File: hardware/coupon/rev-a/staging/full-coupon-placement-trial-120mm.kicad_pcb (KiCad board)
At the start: 2 copper layers, 120 x 32.5 mm, 497 parts, among them J1 USB4505-03-0-A, J2 S2B-PH-SM4-TB, Q1 DMP2066LSN-7, Q10 DMP2066LSN-7, Q11 DMP2066LSN-7, Q12 DMP2066LSN-7, Q13 DMP2066LSN-7, Q14 DMP2066LSN-7, Q15 DMP2066LSN-7, Q16 DMP2066LSN-7, Q17 2N7002K-7, Q18 2N7002K-7, Q19 2N7002K-7, Q2 DMP2066LSN-7, Q20 2N7002K-7, Q21 2N7002K-7, Q22 2N7002K-7, Q23 2N7002K-7, Q24 2N7002K-7, Q25 2N7002K-7, Q26 2N7002K-7, Q27 2N7002K-7, Q28 2N7002K-7, Q29 2N7002K-7, Q3 DMP2066LSN-7, Q30 2N7002K-7, Q31 2N7002K-7, Q32 2N7002K-7, Q4 DMP2066LSN-7, Q5 DMP2066LSN-7, Q6 DMP2066LSN-7, Q7 DMP2066LSN-7, Q8 DMP2066LSN-7, Q9 DMP2066LSN-7, SW1 EVQP7J01P, SW2 JS202011JCQN, U1 TLC59581RTQT, U11 SN74LVC1G04DBVR, U17 SN74LVC1G11DBVR, U2 74HC4514PW,118, U23 SN74LVC1G06DBVR, U24 SN74LVC2G17DBVR, U25 SN74LVC2G17DBVR, U29 TPS70933DBVR, U3 ESP32-S3-WROOM-1U-N16R8, U31 TUSB320LAIRWBR, U32 TS3USB31ERSER, U33 TPD4E05U06DQAR, U34 TPS3808G01DBVR, U35 MAX17048G+T10, U36 TPS631000DRLR, U37 TPS63020DSJT, U38 2.5V shunt, U39 TMP390A2DRLR, U40 SN74AUP1G125DBVR, U41 BQ24074RGTR, U42 SN74AUP1G125DBVR, U43 SN74AUP1G125DBVR, U44 TPS259474ARPWR, U45 TPS259474ARPWR, U46 TCA9517ADGKR, U47 TPS3823A-33DBVR, U48 SN74LVC1G04DSFR, U49 SN74LVC1G74RSER, U50 SN74LVC1G74RSER, U51 SN74LVC1G11DRYR, U52 SN74LVC1G08DSFR, U53 TLV6700DSER, U54 SN74LVC2G00DCUR, U55 SN74LVC2G08DCUR

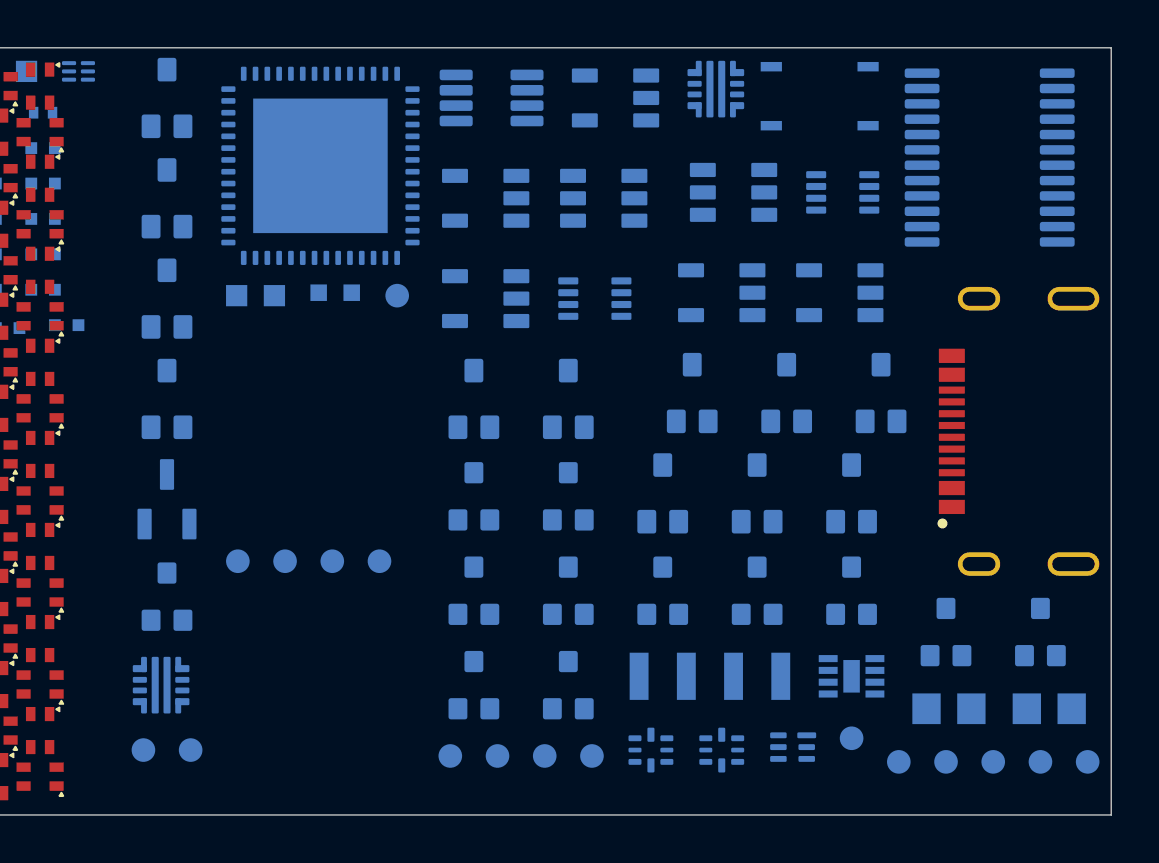
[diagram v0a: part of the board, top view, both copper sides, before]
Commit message: Clear initial placement edge and silkscreen DRC findings
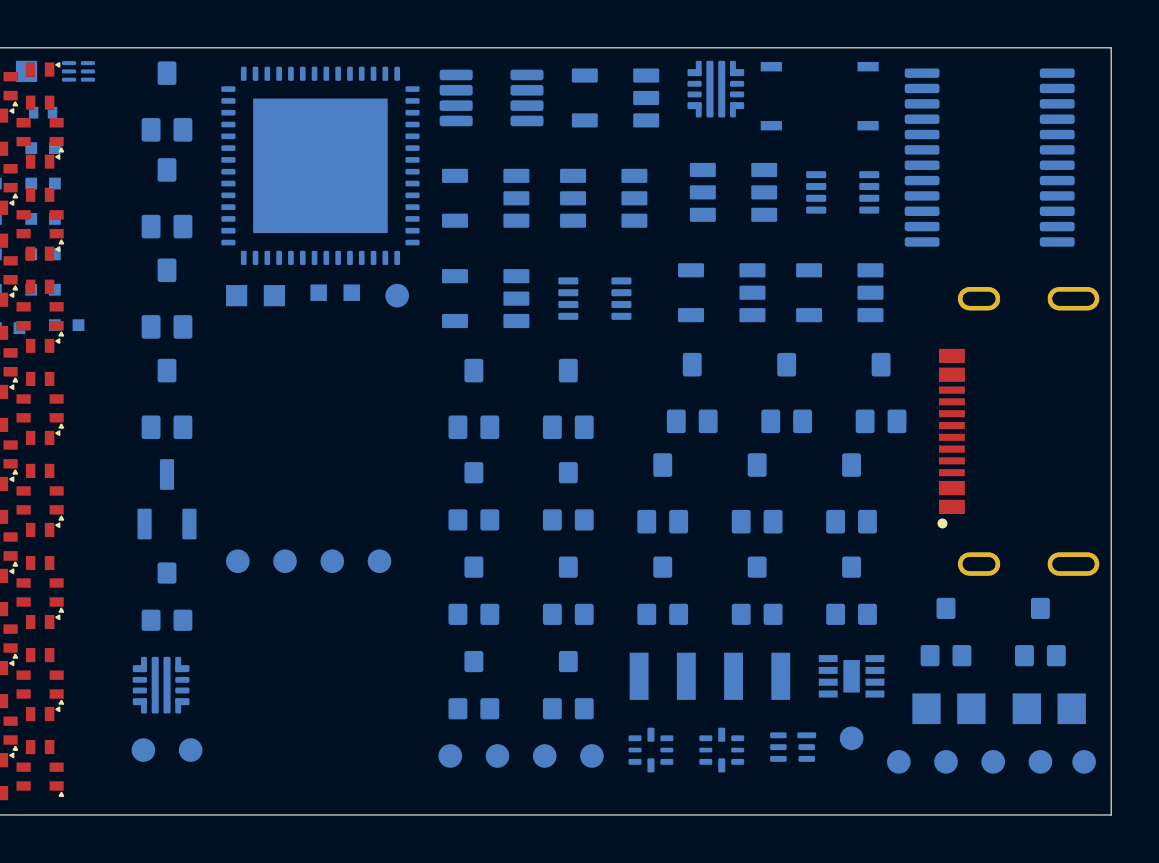
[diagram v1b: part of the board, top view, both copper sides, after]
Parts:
- moved TP4 0.15 mm to (118.9, 30.2)
- moved Q1 0.15 mm to (80.0, 2.27)
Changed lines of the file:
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@@
 	(footprint "rgb-badge-coupon:SC59_Diodes_DMP2066LSN"
 		(layer "B.Cu")
-		(at 80 2.125 180)
+		(at 80 2.275 180)
 		(descr "Diodes Incorporated SC-59 suggested pad layout for DMP2066LSN; SPDX-License-Identifier: CERN-OHL-S-2.0")
 		(property "Reference" "Q1"
@@
 		)
 		(fp_circle
-			(center -2.05 1.25)
-			(end -1.9 1.25)
+			(center -2.05 0.65)
+			(end -1.9 0.65)
 			(stroke
 				(width 0.1)
@@
 	(footprint "rgb-badge-coupon:TestPoint_Pad_D1.0mm"
 		(layer "B.Cu")
-		(at 119.001261 30.25 180)
+		(at 118.851261 30.25 180)
 		(descr "Bare 1.0 mm copper probe pad; no purchased component or solder paste. SPDX-License-Identifier: CERN-OHL-S-2.0")
 		(property "Reference" "TP4"
@@
 		)
 		(fp_circle
-			(center -9.35 8.26)
-			(end -9.15 8.26)
+			(center -9.4 9.15)
+			(end -9.2 9.15)
 			(stroke
 				(width 0.1)

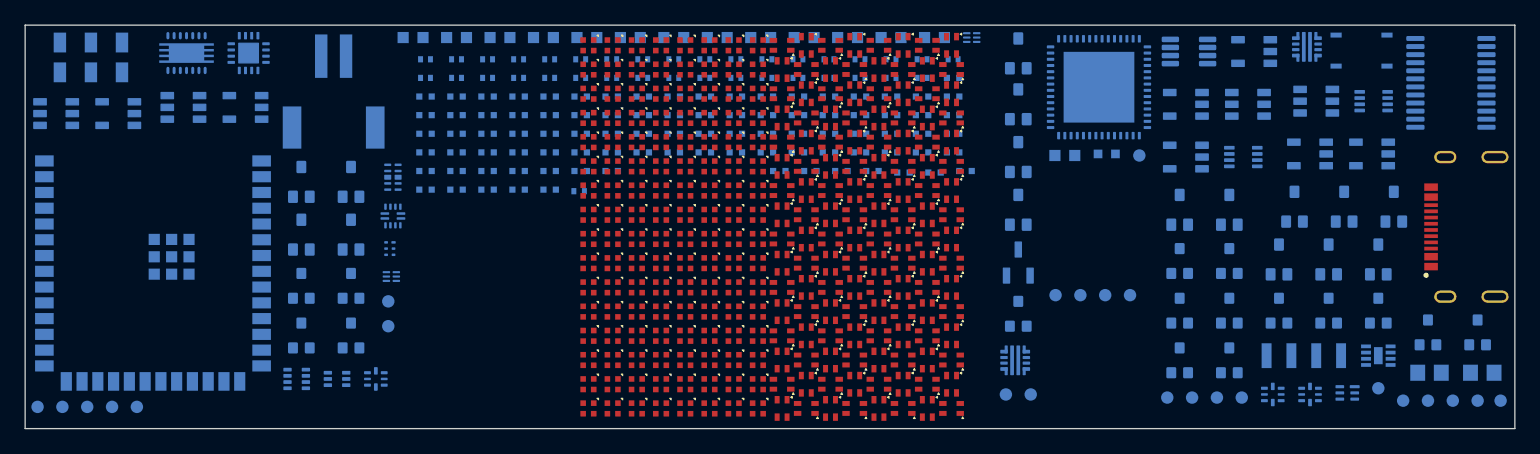
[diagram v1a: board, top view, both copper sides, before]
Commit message: Cluster protected USB stages in full board placement trial
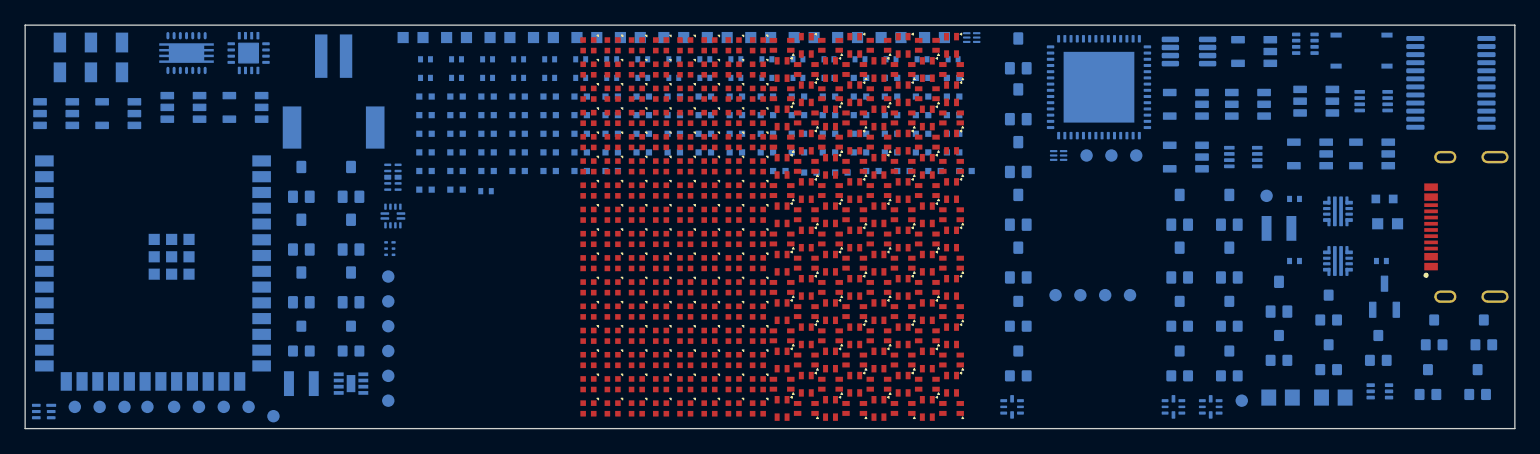
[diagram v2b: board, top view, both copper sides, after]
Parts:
- moved TP33 109.0 mm to (4.00, 30.8)
- moved TP34 109.0 mm to (6.00, 30.8)
- moved TP35 109.0 mm to (8.00, 30.8)
- moved TP4 109.0 mm to (9.85, 30.8)
- moved U53 105.0 mm to (1.50, 31.1)
- moved U36 85.6 mm to (103.1, 1.50)
- moved U39 84.0 mm to (109.1, 29.5)
- moved L2 82.8 mm to (22.2, 28.9)
- moved U35 82.8 mm to (26.2, 28.9)
- moved Q23 78.8 mm to (22.2, 25.2)
- moved Q24 78.8 mm to (26.2, 25.2)
- moved Q7 78.8 mm to (22.2, 21.1)
- moved Q8 78.8 mm to (26.2, 21.1)
- moved Q19 70.8 mm to (93.0, 23.2)
- moved Q20 70.8 mm to (97.0, 23.2)
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
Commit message: Group eFuse programming resistors in board trial
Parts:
- moved C42 99.0 mm to (2.12, 31.0)
- moved C43 99.0 mm to (6.38, 31.0)
- moved TP34 91.8 mm to (97.8, 30.2)
- moved Q21 91.3 mm to (22.2, 25.2)
- moved Q22 91.3 mm to (26.2, 25.2)
- moved Q31 90.8 mm to (22.2, 29.2)
- moved Q32 90.8 mm to (26.2, 29.2)
- moved L2 86.8 mm to (109.0, 29.6)
- moved Q8 83.3 mm to (109.5, 21.9)
- moved Q24 82.8 mm to (109.0, 26.0)
- moved U35 78.8 mm to (105.0, 30.6)
- moved Q23 78.8 mm to (101.0, 26.0)
- moved Q7 78.8 mm to (101.0, 21.9)
- moved U55 75.8 mm to (22.4, 12.6)
- moved Q2 74.8 mm to (97.0, 18.9)
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
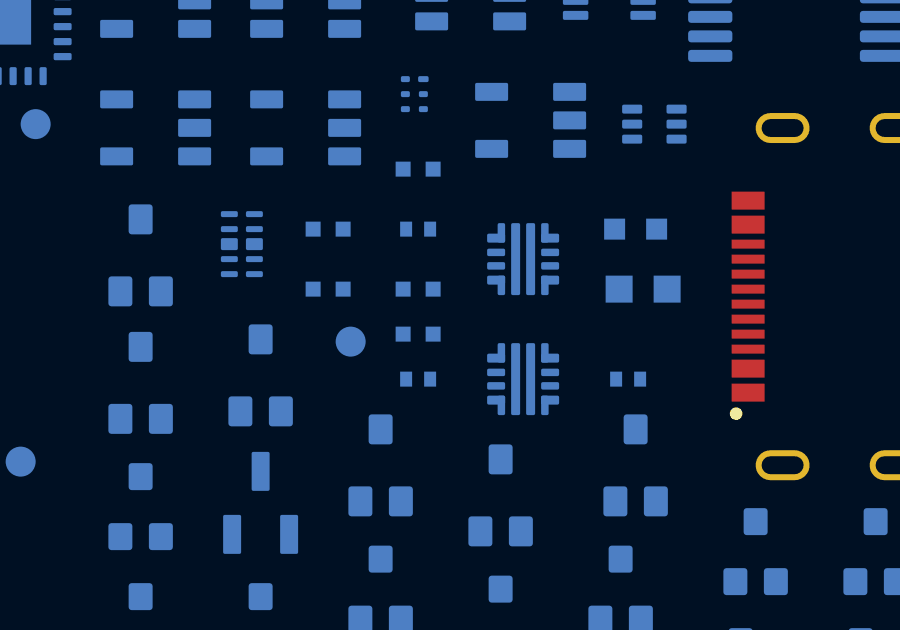
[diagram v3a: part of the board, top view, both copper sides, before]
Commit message: Route four local USB protection support nets in study board
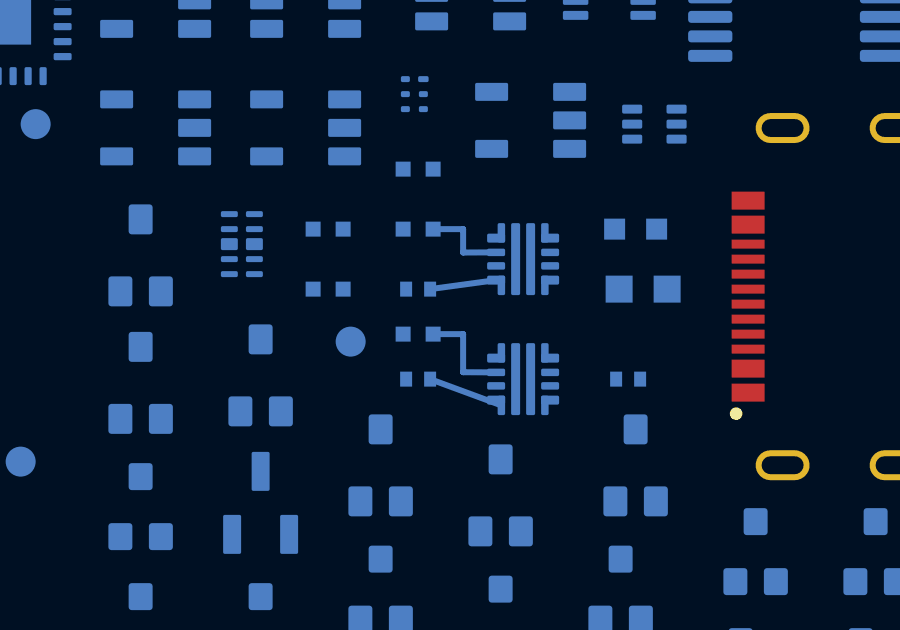
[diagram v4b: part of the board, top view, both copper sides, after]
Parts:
- moved C62 2.00 mm to (102.2, 16.0)
- moved R100 2.00 mm to (102.2, 14.0)
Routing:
- net E1_ILM: track 0.00 -> 3.37 mm
- net E0_ILM: track 0.00 -> 2.88 mm
- net E1_DVDT: track 0.00 -> 2.53 mm
- net E0_DVDT: track 0.00 -> 2.22 mm
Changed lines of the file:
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@@
 	(footprint "rgb-badge-coupon:C_Murata_GRM15_0402"
 		(layer "B.Cu")
-		(at 102.25 14 180)
+		(at 102.25 16 180)
 		(descr "Manufacturer range-based reflow land pattern; SPDX-License-Identifier: CERN-OHL-S-2.0")
 		(property "Reference" "C62"
@@
 	(footprint "rgb-badge-coupon:R_Panasonic_ERJ2_0402"
 		(layer "B.Cu")
-		(at 102.25 16 180)
+		(at 102.25 14 180)
 		(descr "Manufacturer range-based reflow land pattern; SPDX-License-Identifier: CERN-OHL-S-2.0")
 		(property "Reference" "R100"
@@
 		(layer "Edge.Cuts")
 	)
+	(segment
+		(start 102.65 16)
+		(end 104.85 15.7)
+		(width 0.2)
+		(layer "B.Cu")
+		(net "E0_DVDT")
+	)
+	(segment
+		(start 102.75 14)
+		(end 103.75 14)
+		(width 0.2)
+		(layer "B.Cu")
+		(net "E0_ILM")
+	)
+	(segment
+		(start 103.75 14.78)
+		(end 104.85 14.775)
+		(width 0.2)
+		(layer "B.Cu")
+		(net "E0_ILM")
+	)
+	(segment
+		(start 103.75 14)
+		(end 103.75 14.78)
+		(width 0.2)
+		(layer "B.Cu")
+		(net "E0_ILM")
+	)
+	(segment
+		(start 102.65 19)
+		(end 105.025 19.875)
+		(width 0.2)
+		(layer "B.Cu")
+		(net "E1_DVDT")
+	)
+	(segment
+		(start 103.75 17.5)
+		(end 103.75 18.77)
+		(width 0.2)
+		(layer "B.Cu")
+		(net "E1_ILM")
+	)
+	(segment
+		(start 103.75 18.77)
+		(end 104.85 18.775)
+		(width 0.2)
+		(layer "B.Cu")
+		(net "E1_ILM")
+	)
+	(segment
+		(start 102.75 17.5)
+		(end 103.75 17.5)
+		(width 0.2)
+		(layer "B.Cu")
+		(net "E1_ILM")
+	)
 	(embedded_fonts no)

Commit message: Use planned six-layer provisional stack in PCB study
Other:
- copper layers 2 -> 6
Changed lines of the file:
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@@
 	(generator_version "10.0")
 	(general
-		(thickness 1.6)
+		(thickness 1)
 		(legacy_teardrops no)
 	)
@@
 	(layers
 		(0 "F.Cu" signal)
+		(4 "In1.Cu" signal)
+		(6 "In2.Cu" signal)
+		(8 "In3.Cu" signal)
+		(10 "In4.Cu" signal)
 		(2 "B.Cu" signal)
 		(9 "F.Adhes" user "F.Adhesive")
@@
 	)
 	(segment
-		(start 102.75 14)
-		(end 103.75 14)
+		(start 103.75 14)
+		(end 103.75 14.78)
 		(width 0.2)
 		(layer "B.Cu")
@@
 	)
 	(segment
-		(start 103.75 14)
-		(end 103.75 14.78)
+		(start 102.75 14)
+		(end 103.75 14)
 		(width 0.2)
 		(layer "B.Cu")
@@
 	)
 	(segment
-		(start 103.75 17.5)
-		(end 103.75 18.77)
+		(start 102.75 17.5)
+		(end 103.75 17.5)
 		(width 0.2)
 		(layer "B.Cu")
@@
 	)
 	(segment
-		(start 102.75 17.5)
-		(end 103.75 17.5)
+		(start 103.75 17.5)
+		(end 103.75 18.77)
 		(width 0.2)
 		(layer "B.Cu")

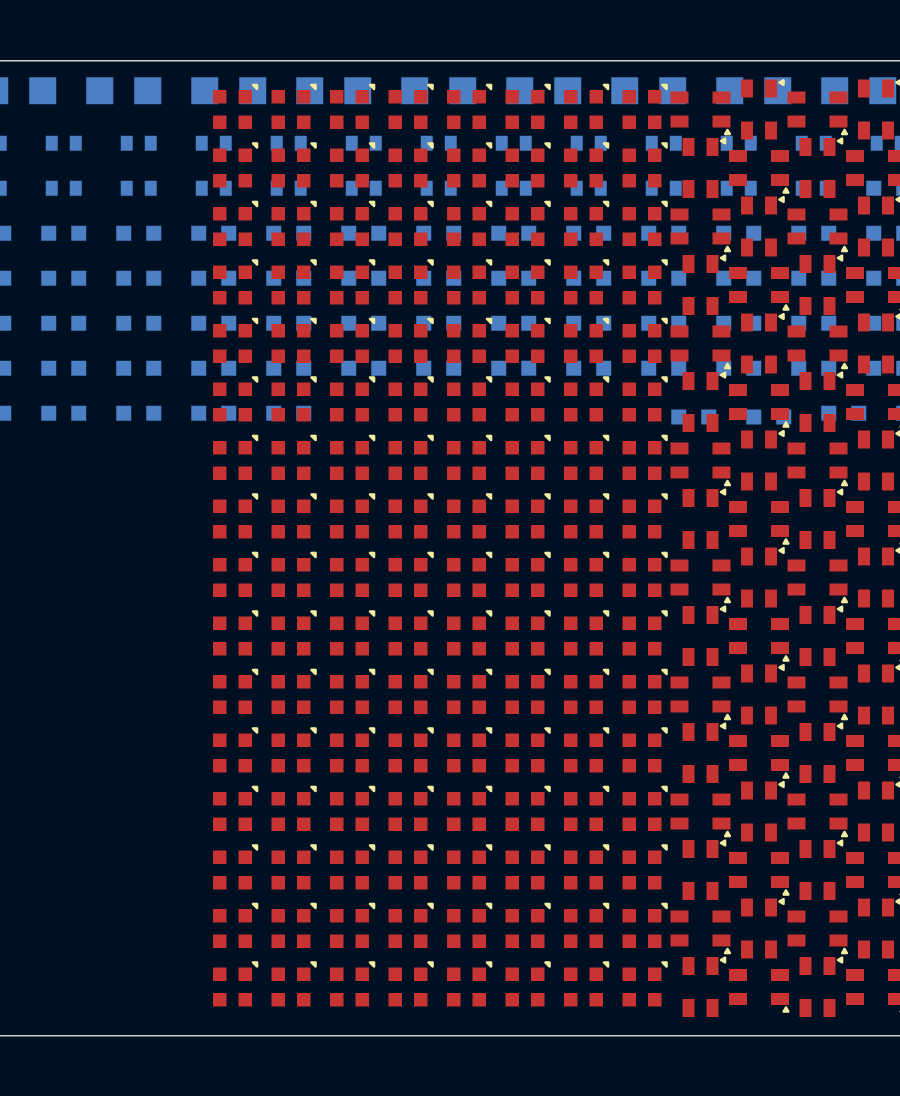
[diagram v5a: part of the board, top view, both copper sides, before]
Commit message: Route Everlight half-row anodes in six-layer board study
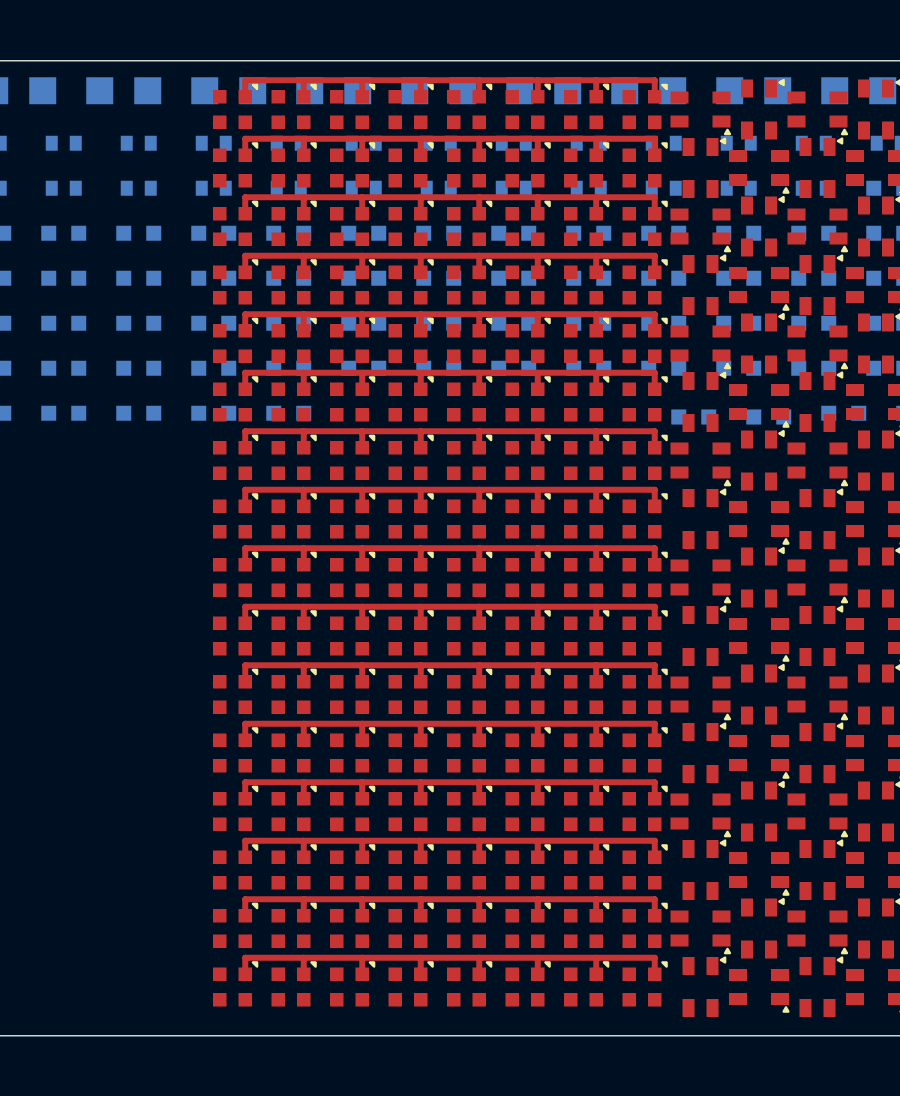
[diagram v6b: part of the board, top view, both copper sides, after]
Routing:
- net ROW_15_A: track 0.00 -> 18.1 mm
- net ROW_14_A: track 0.00 -> 18.1 mm
- net ROW_13_A: track 0.00 -> 18.1 mm
- net ROW_12_A: track 0.00 -> 18.1 mm
- net ROW_10_A: track 0.00 -> 18.1 mm
- net ROW_09_A: track 0.00 -> 18.1 mm
- net ROW_08_A: track 0.00 -> 18.1 mm
- net ROW_06_A: track 0.00 -> 18.1 mm
- net ROW_04_A: track 0.00 -> 18.1 mm
- net ROW_01_A: track 0.00 -> 18.1 mm
- net ROW_02_A: track 0.00 -> 18.1 mm
- net ROW_03_A: track 0.00 -> 18.1 mm
- net ROW_00_A: track 0.00 -> 18.1 mm
- net ROW_07_A: track 0.00 -> 18.0 mm
- net ROW_05_A: track 0.00 -> 18.0 mm
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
